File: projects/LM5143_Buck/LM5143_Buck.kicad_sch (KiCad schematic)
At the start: 125 parts, among them J1 Bat In, J2 24V Out, J3 I2C Socket, J4 I2C Socket, Q1 IGC025S08S1, Q2 IGC025S08S1, Q3 IGC025S08S1, Q4 IGC025S08S1, SW1 SW_SPDT, SW2 SW_SPDT, SW3 Addr_Switch, SW4 Addr_Switch, U2 LM5113-Q1, U3 LM5113-Q1, U4 TLV74033, U5 AP7387-50FDC-7, U6 INA226

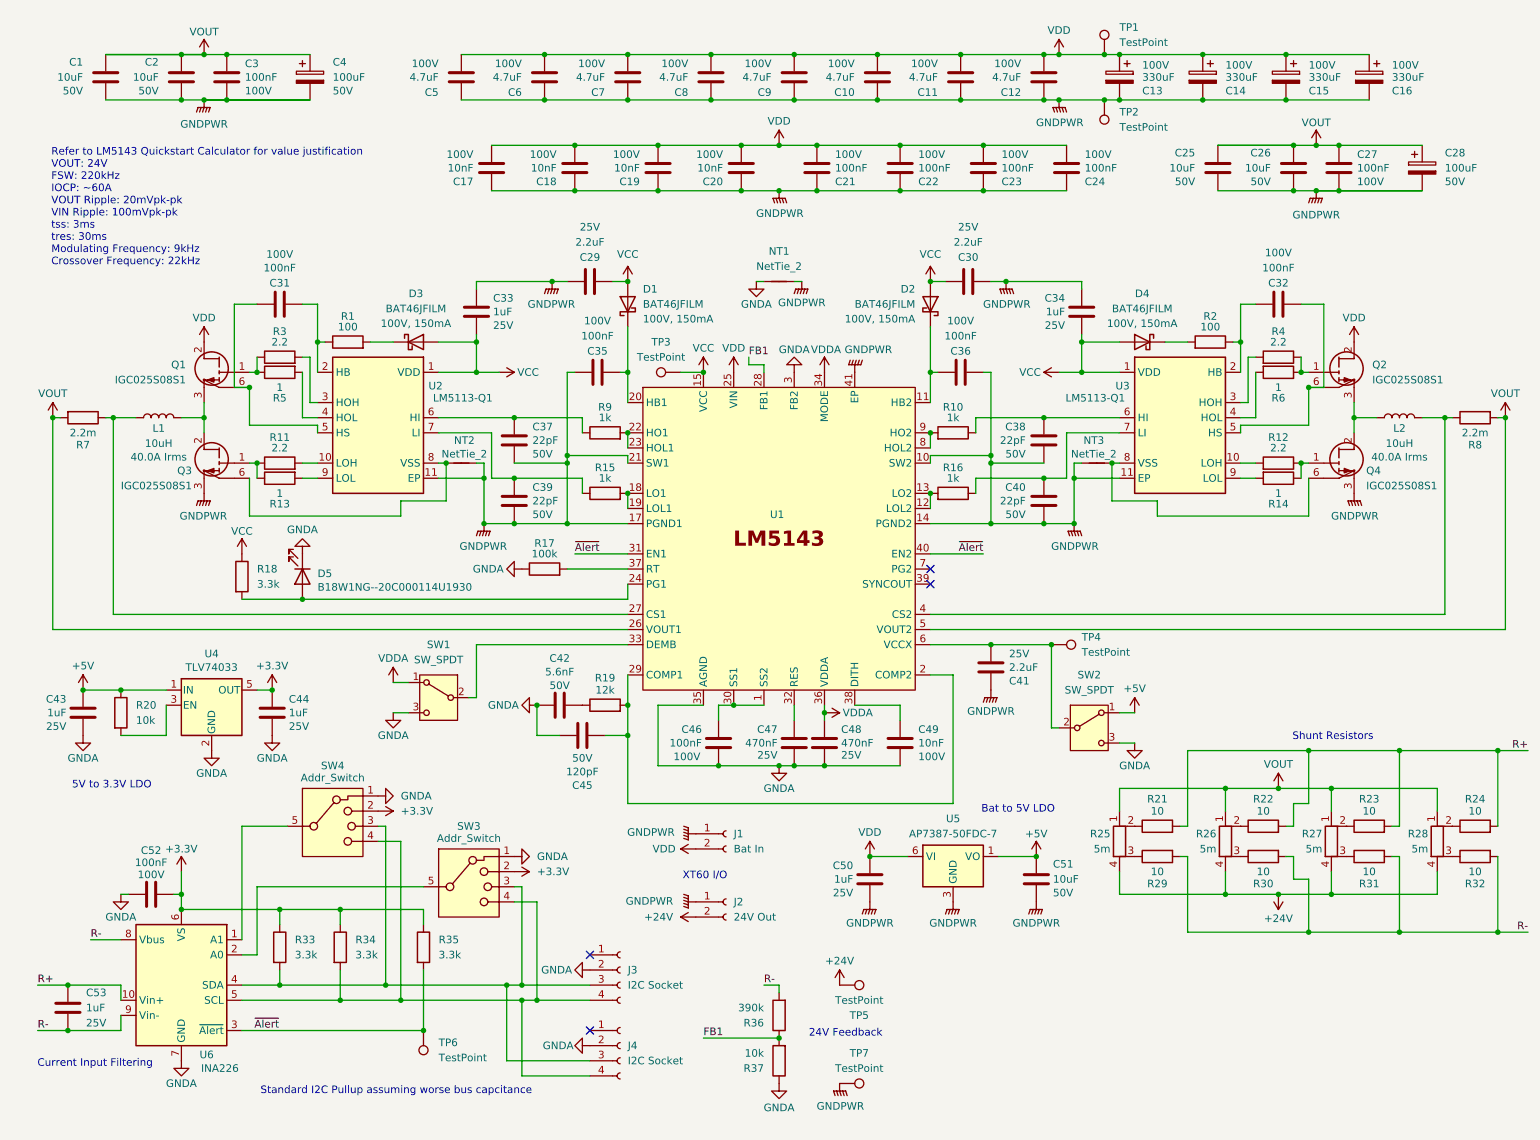
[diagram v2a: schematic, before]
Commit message: Added more capacitors
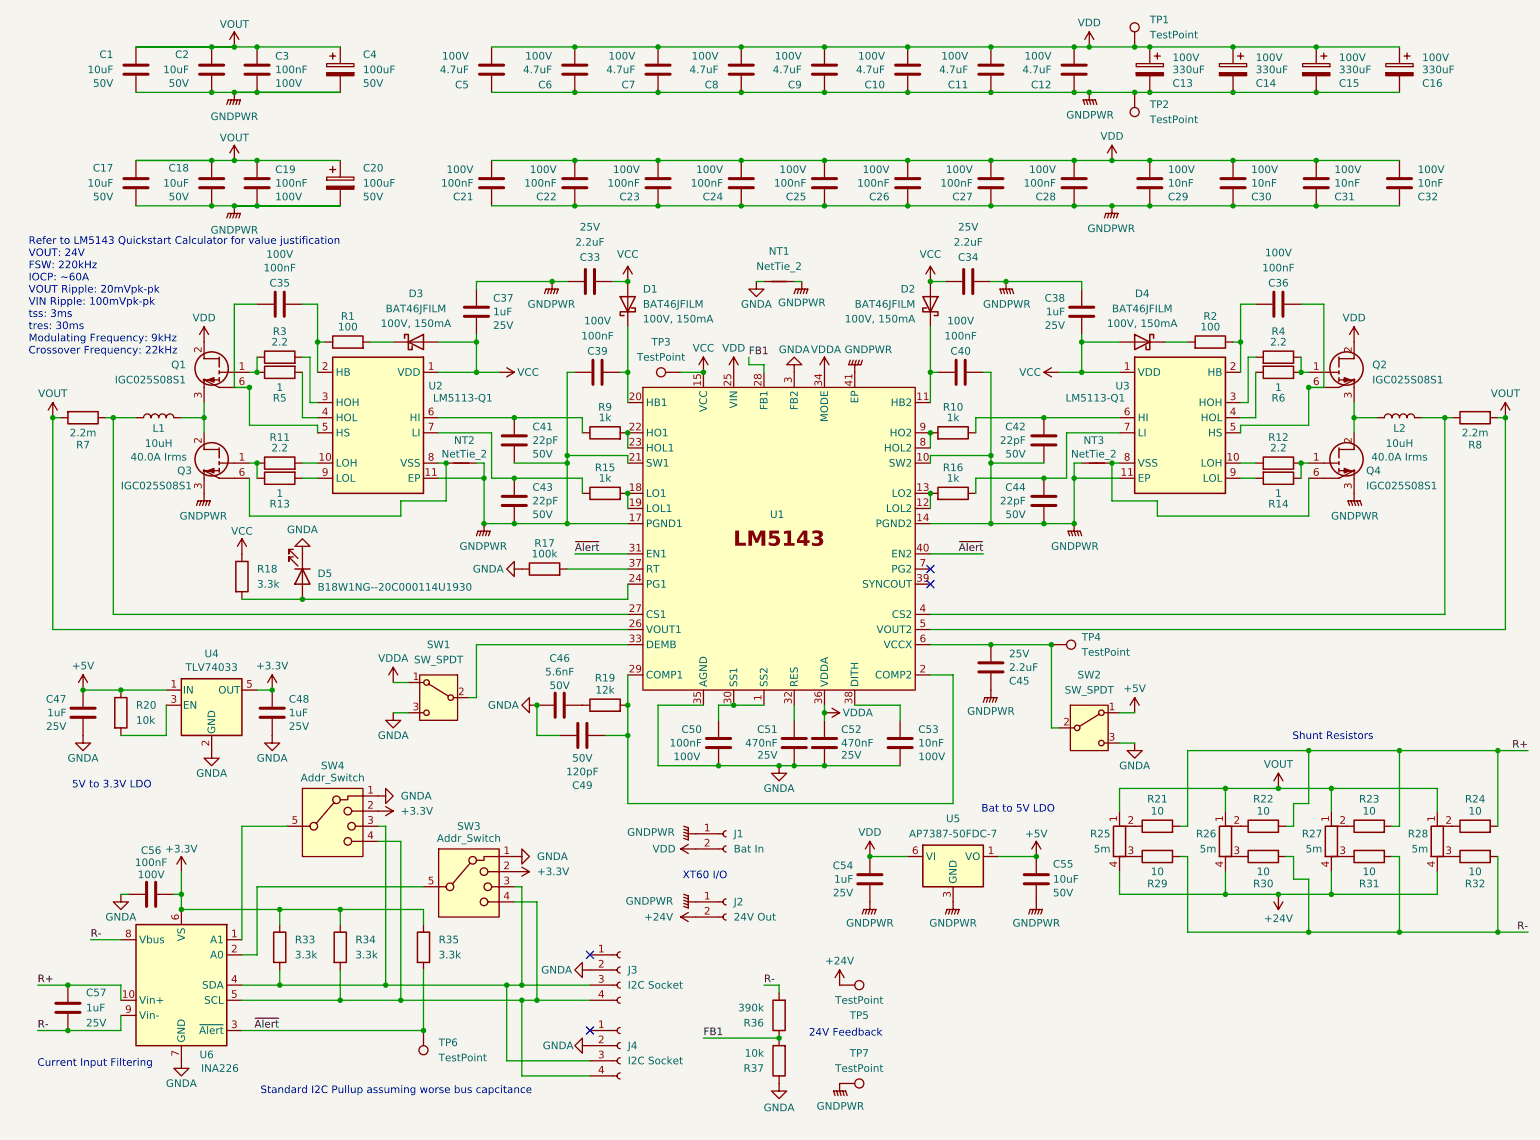
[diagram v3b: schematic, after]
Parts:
- added C21, C22, C23, C24: 100nF, Capacitor_SMD:C_0603_1608Metric, symbol Device:C
- renumbered C25 to C17, C26 to C18, C27 to C19, C28 to C20, C24 to C25, C23 to C26, C22 to C27, C21 to C28, C20 to C29, C19 to C30, C18 to C31, C17 to C32, C29 to C33, C30 to C34, C31 to C35, C32 to C36, C33 to C37, C34 to C38, C35 to C39, C36 to C40, C37 to C41, C38 to C42, C39 to C43, C40 to C44, C41 to C45, C42 to C46, C43 to C47, C44 to C48, C45 to C49, C46 to C50, C47 to C51, C48 to C52, C49 to C53, C50 to C54, C51 to C55, C52 to C56, C53 to C57
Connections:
- net GND: now also C21.1, C22.1, C23.1, C24.1
- net VDD: now also C21.2, C22.2, C23.2, C24.2
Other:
- moved on the sheet: C1, C10, C11, C12, C13, C14, C15, C16, C17, C18, C19, C2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

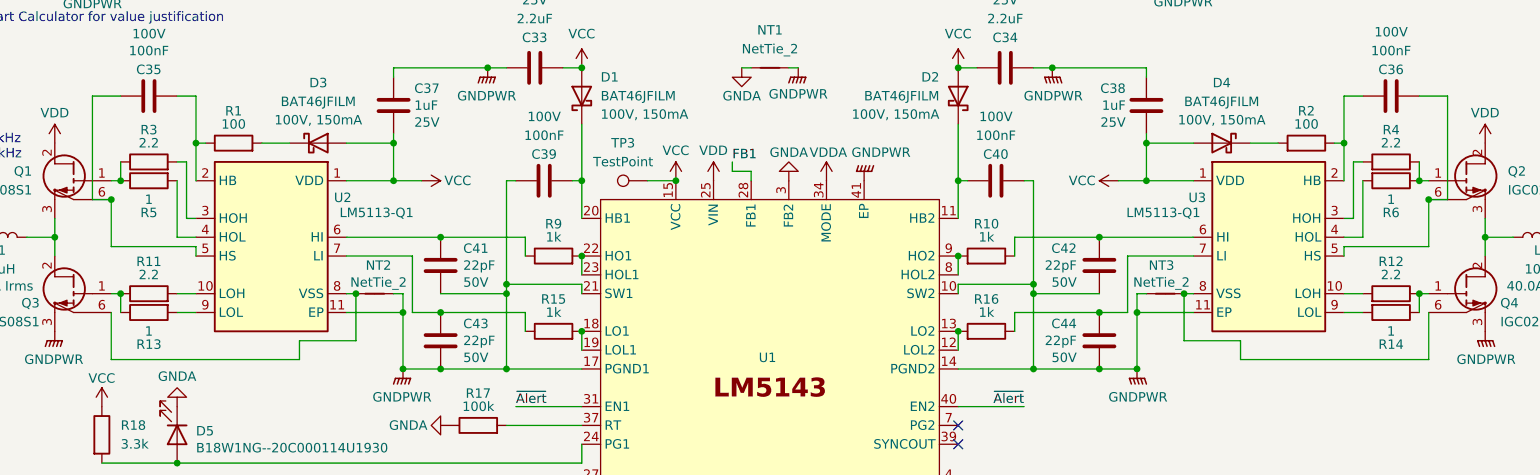
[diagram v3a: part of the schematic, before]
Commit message: Add via stitching
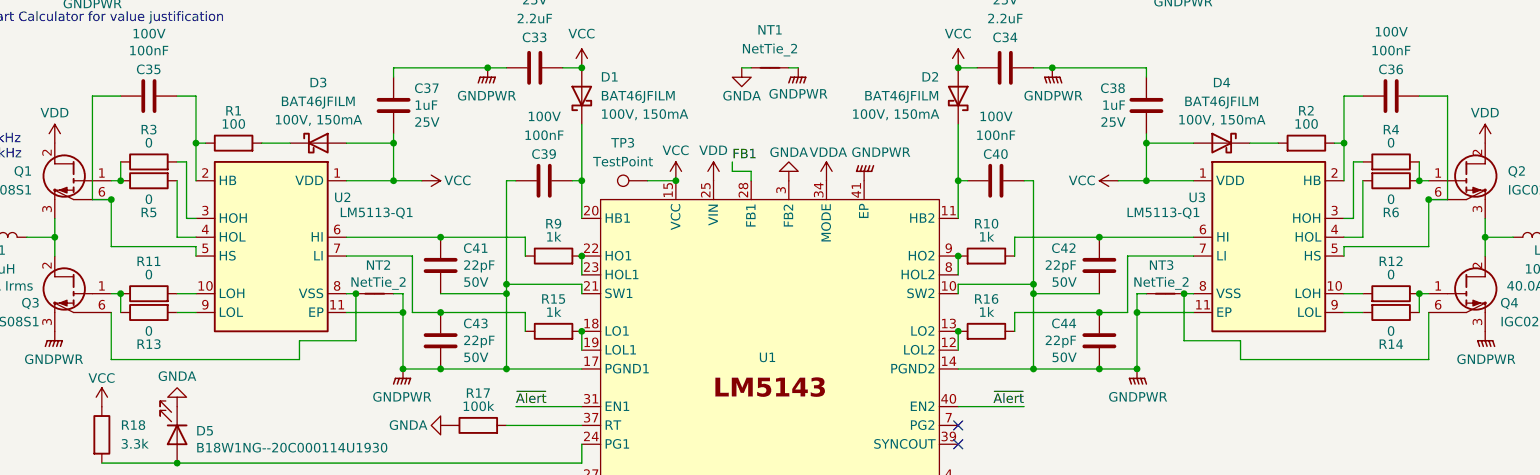
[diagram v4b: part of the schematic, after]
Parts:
- R11, R12, R3, R4: value 2.2 -> 0
- R13, R14, R5, R6: value 1 -> 0
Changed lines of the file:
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@@
 			)
 		)
-		(property "Value" "2.2"
+		(property "Value" "0"
 			(at 55.88 87.63 90)
 			(effects
@@
 			)
 		)
-		(property "Datasheet" "https://www.lcsc.com/product-detail/C728638.html"
+		(property "Datasheet" ""
 			(at 55.88 90.17 0)
 			(effects
@@
 			)
 		)
-		(property "Value" "2.2"
+		(property "Value" "0"
 			(at 55.88 69.85 90)
 			(effects
@@
 			)
 		)
-		(property "Datasheet" "https://www.lcsc.com/product-detail/C728638.html"
+		(property "Datasheet" ""
 			(at 55.88 72.39 0)
 			(effects
@@
 			)
 		)
-		(property "Value" "2.2"
+		(property "Value" "0"
 			(at 223.52 69.85 90)
 			(effects
@@
 			)
 		)
-		(property "Datasheet" "https://www.lcsc.com/product-detail/C728638.html"
+		(property "Datasheet" ""
 			(at 223.52 72.39 0)
 			(effects
@@
 			)
 		)
-		(property "Value" "1"
+		(property "Value" "0"
 			(at 223.52 95.25 90)
 			(effects
@@
 			)
 		)
-		(property "Datasheet" "https://www.lcsc.com/product-detail/C728638.html"
+		(property "Datasheet" ""
 			(at 223.52 92.71 0)
 			(effects
@@
 			)
 		)
-		(property "Value" "1"
+		(property "Value" "0"
 			(at 223.52 77.47 90)
 			(effects
@@
 			)
 		)
-		(property "Datasheet" "https://www.lcsc.com/product-detail/C728638.html"
+		(property "Datasheet" ""
 			(at 223.52 74.93 0)
 			(effects
@@
 			)
 		)
-		(property "Value" "1"
+		(property "Value" "0"
 			(at 55.88 95.25 90)
 			(effects
@@
 			)
 		)
-		(property "Datasheet" "https://www.lcsc.com/product-detail/C728638.html"
+		(property "Datasheet" ""
 			(at 55.88 92.71 0)
 			(effects
@@
 			)
 		)
-		(property "Value" "1"
+		(property "Value" "0"
 			(at 55.88 77.47 90)
 			(effects
@@
 			)
 		)
-		(property "Datasheet" "https://www.lcsc.com/product-detail/C728638.html"
+		(property "Datasheet" ""
 			(at 55.88 74.93 0)
 			(effects
@@
 			)
 		)
-		(property "Value" "2.2"
+		(property "Value" "0"
 			(at 223.52 87.63 90)
 			(effects
@@
 			)
 		)
-		(property "Datasheet" "https://www.lcsc.com/product-detail/C728638.html"
+		(property "Datasheet" ""
 			(at 223.52 90.17 0)
 			(effects
